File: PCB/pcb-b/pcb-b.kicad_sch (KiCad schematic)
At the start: 25 parts, among them J1 Conn_02x05_Counter_Clockwise, J2 Conn_02x05_Counter_Clockwise, K1 HK19F-DCxxV-SHC, Q13 TPCA8120,L1Q, Q3 BC817, Q9 BC817

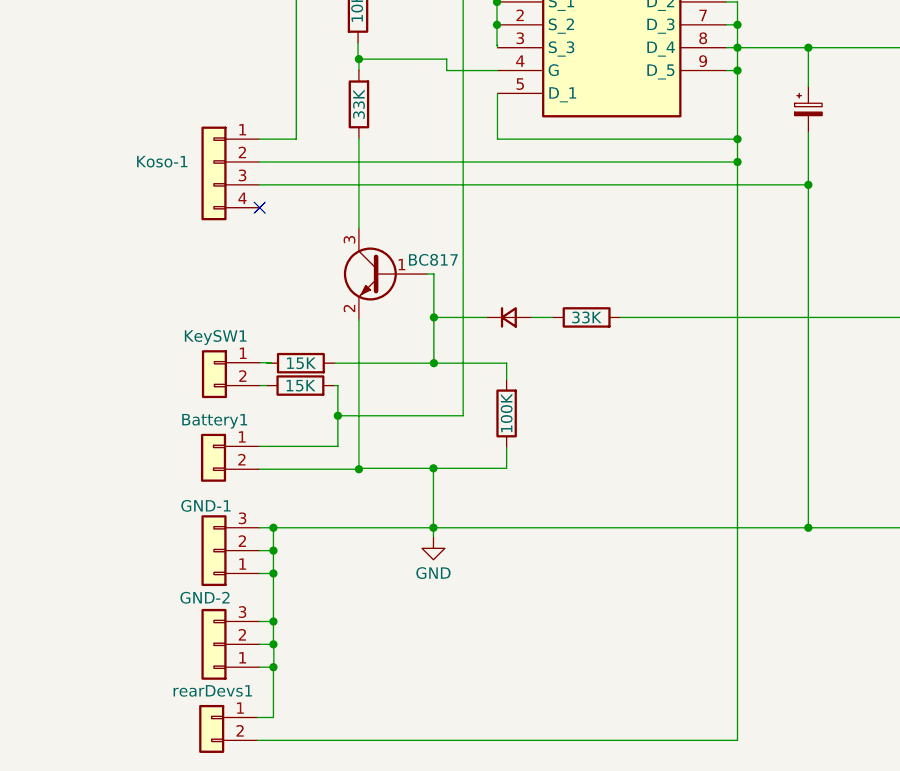
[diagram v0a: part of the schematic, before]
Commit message: Enhancements and size reduction
- Because the day-light needs just low current (<=500 mA), it no more uses the passive fuse. It has been replaced by a
  MSMF050-2 electronic fuse. Less passive fuses means less electric wires, then less chaos!
- A better components space distribution has reduced the PCB size (40.00mm x 90.11mm)
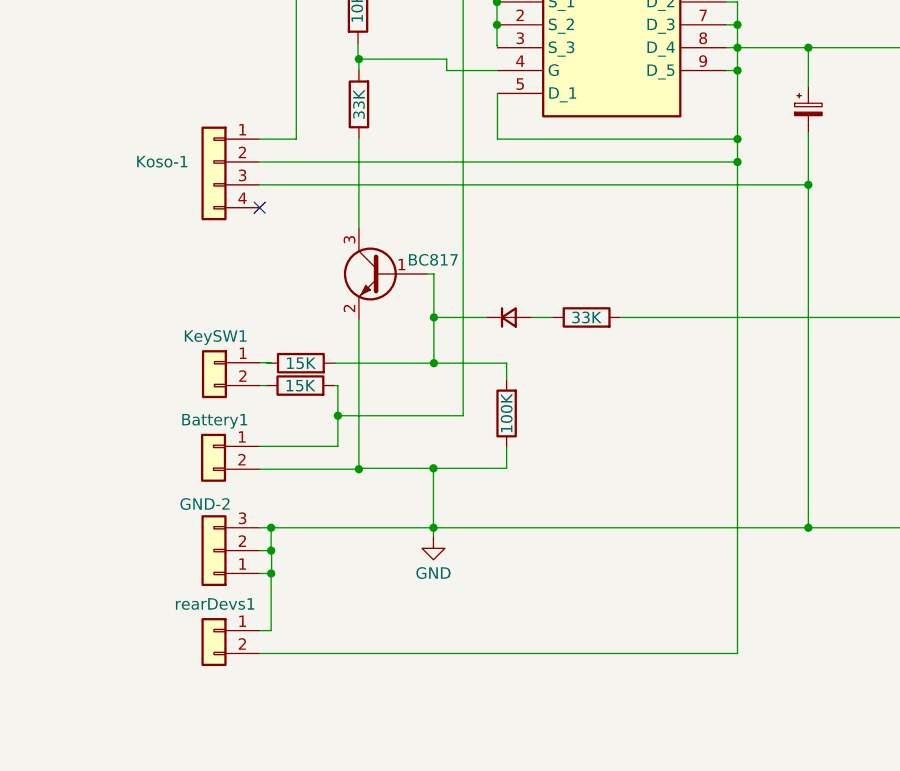
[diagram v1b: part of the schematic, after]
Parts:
- removed GND-1: ~, Connector_Wire:SolderWire-1sqmm_1x03_P5.4mm_D1.4mm_OD2.7mm, symbol Connector_Generic:Conn_01x03
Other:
- moved on the sheet: GND-2, rearDevs1
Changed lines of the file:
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@@
 	)
 	(junction
-		(at 45.72 169.164)
+		(at 45.466 158.75)
 		(diameter 0)
 		(color 0 0 0 0)
@@
 	)
 	(junction
-		(at 45.72 161.29)
-		(diameter 0)
-		(color 0 0 0 0)
-	)
-	(junction
 		(at 197.104 115.316)
 		(diameter 0)
@@
 	)
 	(junction
-		(at 45.72 158.75)
-		(diameter 0)
-		(color 0 0 0 0)
-	)
-	(junction
 		(at 70.5612 100.33)
 		(diameter 0)
@@
 	)
 	(junction
-		(at 45.72 174.244)
+		(at 45.466 163.83)
 		(diameter 0)
 		(color 0 0 0 0)
@@
 	)
 	(junction
-		(at 45.72 171.704)
+		(at 45.466 161.29)
 		(diameter 0)
 		(color 0 0 0 0)
@@
 	)
 	(junction
-		(at 45.72 163.83)
-		(diameter 0)
-		(color 0 0 0 0)
-	)
-	(junction
 		(at 149.86 135.382)
 		(diameter 0)
@@
 	(wire
 		(pts
-			(xy 45.72 161.29) (xy 45.72 163.83)
-		)
-		(stroke
-			(width 0)
-			(type default)
-		)
-	)
-	(wire
-		(pts
 			(xy 55.118 96.266) (xy 67.056 96.266)
 		)
@@
 	(wire
 		(pts
-			(xy 45.72 158.75) (xy 63.5 158.75)
-		)
-		(stroke
-			(width 0)
-			(type default)
-		)
-	)
-	(wire
-		(pts
 			(xy 107.696 77.47) (xy 107.696 77.724)
 		)
@@
 	(wire
 		(pts
-			(xy 45.72 174.244) (xy 45.7708 174.244)
+			(xy 45.466 163.83) (xy 45.5168 163.83)
 		)
 		(stroke
@@
 	(wire
 		(pts
-			(xy 116.1288 59.436) (xy 119.888 59.436)
+			(xy 45.466 158.75) (xy 63.5 158.75)
 		)
 		(stroke
@@
 	(wire
 		(pts
-			(xy 147.32 54.102) (xy 147.32 54.356)
+			(xy 116.1288 59.436) (xy 119.888 59.436)
 		)
 		(stroke
@@
 	(wire
 		(pts
-			(xy 105.156 114.808) (xy 105.156 120.65)
+			(xy 147.32 54.102) (xy 147.32 54.356)
 		)
 		(stroke
@@
 	(wire
 		(pts
-			(xy 106.934 80.01) (xy 119.888 80.01)
+			(xy 105.156 114.808) (xy 105.156 120.65)
 		)
 		(stroke
@@
 	(wire
 		(pts
-			(xy 45.72 158.75) (xy 45.72 161.29)
+			(xy 106.934 80.01) (xy 119.888 80.01)
 		)
 		(stroke
@@
 	(wire
 		(pts
-			(xy 44.196 174.244) (xy 45.72 174.244)
+			(xy 44.196 163.83) (xy 45.466 163.83)
 		)
 		(stroke
@@
 	(wire
 		(pts
-			(xy 45.72 169.164) (xy 45.72 171.704)
+			(xy 45.466 158.75) (xy 45.466 161.29)
 		)
 		(stroke
@@
 	(wire
 		(pts
-			(xy 44.196 171.704) (xy 45.72 171.704)
+			(xy 44.196 161.29) (xy 45.466 161.29)
 		)
 		(stroke
@@
 	(wire
 		(pts
-			(xy 97.282 182.372) (xy 43.942 182.372)
+			(xy 97.282 172.72) (xy 44.196 172.72)
 		)
 		(stroke
@@
 	(wire
 		(pts
-			(xy 45.72 179.832) (xy 45.72 174.244)
+			(xy 45.466 170.18) (xy 45.466 163.83)
 		)
 		(stroke
@@
 	(wire
 		(pts
-			(xy 45.7708 171.8564) (xy 45.72 171.8564)
+			(xy 45.5168 161.4424) (xy 45.466 161.4424)
 		)
 		(stroke
@@
 	(wire
 		(pts
-			(xy 44.196 161.29) (xy 45.72 161.29)
-		)
-		(stroke
-			(width 0)
-			(type default)
-		)
-	)
-	(wire
-		(pts
 			(xy 149.86 75.184) (xy 151.13 75.184)
 		)
@@
 	(wire
 		(pts
-			(xy 45.72 171.704) (xy 45.72 171.8564)
+			(xy 45.466 161.29) (xy 45.466 161.4424)
 		)
 		(stroke
@@
 	(wire
 		(pts
-			(xy 45.72 163.83) (xy 45.72 169.164)
-		)
-		(stroke
-			(width 0)
-			(type default)
-		)
-	)
-	(wire
-		(pts
 			(xy 102.616 64.262) (xy 113.538 64.262)
 		)
@@
 	(wire
 		(pts
-			(xy 44.196 169.164) (xy 45.72 169.164)
+			(xy 44.196 158.75) (xy 45.466 158.75)
 		)
 		(stroke
@@
 	(wire
 		(pts
-			(xy 43.942 179.832) (xy 45.72 179.832)
+			(xy 44.196 170.18) (xy 45.466 170.18)
 		)
 		(stroke
@@
 	(wire
 		(pts
-			(xy 97.282 118.11) (xy 97.282 182.372)
-		)
-		(stroke
-			(width 0)
-			(type default)
-		)
-	)
-	(wire
-		(pts
-			(xy 44.196 158.75) (xy 45.72 158.75)
+			(xy 97.282 118.11) (xy 97.282 172.72)
 		)
 		(stroke
@@
 	(wire
 		(pts
-			(xy 44.196 163.83) (xy 45.72 163.83)
-		)
-		(stroke
-			(width 0)
-			(type default)
-		)
-	)
-	(wire
-		(pts
-			(xy 45.7708 174.244) (xy 45.7708 171.8564)
+			(xy 45.5168 163.83) (xy 45.5168 161.4424)
 		)
 		(stroke
@@
 	)
 	(symbol
-		(lib_id "Connector_Generic:Conn_01x03")
-		(at 39.116 161.29 180)
-		(unit 1)
-		(exclude_from_sim no)
-		(in_bom yes)
-		(on_board yes)
-		(dnp no)
-		(property "Reference" "GND-1"
-			(at 38.2524 156.3624 0)
-			(effects
-				(font
-					(size 1.27 1.27)
-				)
-			)
-		)
-		(property "Value" "~"
-			(at 39.1668 156.4132 0)
-			(effects
-				(font
-					(size 1.27 1.27)
-				)
-				(hide yes)
-			)
-		)
-		(property "Footprint" "Connector_Wire:SolderWire-1sqmm_1x03_P5.4mm_D1.4mm_OD2.7mm"
-			(at 39.116 161.29 0)
-			(effects
-				(font
-					(size 1.27 1.27)
-				)
-				(hide yes)
-			)
-		)
-		(property "Datasheet" "~"
-			(at 39.116 161.29 0)
-			(effects
-				(font
-					(size 1.27 1.27)
-				)
-				(hide yes)
-			)
-		)
-		(property "Description" ""
-			(at 39.116 161.29 0)
-			(effects
-				(font
-					(size 1.27 1.27)
-				)
-				(hide yes)
-			)
-		)
-		(pin "2"
-		)
-		(pin "1"
-		)
-		(pin "3"
-		)
-		(instances
-			(project "pcb-b"
-				(path "/709d0967-afe5-49d3-92a5-d2bb94550bdb"
-					(reference "GND-1")
-					(unit 1)
-				)
-			)
-		)
-	)
-	(symbol
 		(lib_id "Device:R")
 		(at 149.86 147.574 180)
@@
 	(symbol
 		(lib_id "Connector_Generic:Conn_01x02")
-		(at 38.862 179.832 0)
+		(at 39.116 170.18 0)
 		(mirror y)
 		(unit 1)
@@
 		(dnp no)
 		(property "Reference" "rearDevs1"
-			(at 38.989 176.911 0)
+			(at 39.243 167.259 0)
 			(effects
 				(font
@@
 		)
 		(property "Value" "Conn_01x02"
-			(at 38.862 176.276 0)
+			(at 39.116 166.624 0)
 			(effects
 				(font
@@
 		)
 		(property "Footprint" "Connector_PinHeader_2.54mm:PinHeader_1x02_P2.54mm_Vertical"
-			(at 38.862 179.832 0)
+			(at 39.116 170.18 0)
 			(effects
 				(font
@@
 		)
 		(property "Datasheet" "~"
-			(at 38.862 179.832 0)
+			(at 39.116 170.18 0)
 			(effects
 				(font
@@
 		)
 		(property "Description" ""
-			(at 38.862 179.832 0)
+			(at 39.116 170.18 0)
 			(effects
 				(font
@@
 	(symbol
 		(lib_id "Connector_Generic:Conn_01x03")
-		(at 39.116 171.704 180)
+		(at 39.116 161.29 180)
 		(unit 1)
 		(exclude_from_sim no)
@@
 		(dnp no)
 		(property "Reference" "GND-2"
-			(at 38.1508 166.5732 0)
+			(at 38.1508 156.1592 0)
 			(effects
 				(font
@@
 		)
 		(property "Value" "~"
-			(at 39.1668 166.8272 0)
+			(at 39.1668 156.4132 0)
 			(effects
 				(font
@@
 		)
 		(property "Footprint" "Connector_Wire:SolderWire-0.75sqmm_1x03_P4.8mm_D1.25mm_OD2.3mm"
-			(at 39.116 171.704 0)
+			(at 39.116 161.29 0)
 			(effects
 				(font
@@
 		)
 		(property "Datasheet" "~"
-			(at 39.116 171.704 0)
+			(at 39.116 161.29 0)
 			(effects
 				(font
@@
 		)
 		(property "Description" ""
-			(at 39.116 171.704 0)
+			(at 39.116 161.29 0)
 			(effects
 				(font

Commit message: Battery connector-wire size changed
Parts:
- Battery1: footprint Connector_Wire:SolderWire-0.75sqmm_1x02_P7mm_D1.25mm_OD3.5mm -> Connector_Wire:SolderWire-1sqmm_1x02_P5.4mm_D1.4mm_OD2.7mm
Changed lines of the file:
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@@
 			)
 		)
-		(property "Footprint" "Connector_Wire:SolderWire-0.75sqmm_1x02_P7mm_D1.25mm_OD3.5mm"
+		(property "Footprint" "Connector_Wire:SolderWire-1sqmm_1x02_P5.4mm_D1.4mm_OD2.7mm"
 			(at 39.0652 149.7076 0)
 			(effects

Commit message: PCB(b) size reduction and unuseful resistors removed
Originally, I placed resistors between the MOSFET's gate and the NPN collector to reduce the possible VGS voltage difference.
But, reading the TCPA8120's datasheet I have seen it accepts VGS max -20!! But in motorbike battey I never see 20 volts. So,
I removed the resistors. Now, when the NPN is conducing then the VGS will be about -12 volts, it is also better to avoid the
MOSFETs work in linear mode.

Thank to this component removing, also the PCB size has been reduced (85.6mm x 40.0mm). But, in order to get the size reduction
the add-light connector has been splitted in two single wite connectors. It is not beautiful to see, bet the PCB size is a too
big problem, and multilayer solution is a too expensive one!
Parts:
- removed R3: 33K, Resistor_SMD:R_1206_3216Metric, symbol Device:R
- R2: value 10K -> 15K
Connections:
- net at Q13.4 (G), R2.2: now also Q9.3 (C)
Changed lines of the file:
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@@
 	)
 	(junction
+		(at 55.372 96.266)
+		(diameter 0)
+		(color 0 0 0 0)
+	)
+	(junction
 		(at 241.554 130.556)
 		(diameter 0)
@@
 	)
 	(junction
-		(at 45.466 163.83)
+		(at 55.2704 152.2476)
 		(diameter 0)
 		(color 0 0 0 0)
 	)
 	(junction
-		(at 145.288 59.69)
+		(at 45.466 163.83)
 		(diameter 0)
 		(color 0 0 0 0)
 	)
 	(junction
-		(at 45.466 161.29)
+		(at 145.288 59.69)
 		(diameter 0)
 		(color 0 0 0 0)
 	)
 	(junction
-		(at 63.5508 140.462)
+		(at 45.466 161.29)
 		(diameter 0)
 		(color 0 0 0 0)
 	)
 	(junction
-		(at 55.118 96.266)
+		(at 63.5508 140.462)
 		(diameter 0)
 		(color 0 0 0 0)
@@
 	)
 	(junction
-		(at 97.282 118.11)
+		(at 55.372 106.68)
 		(diameter 0)
 		(color 0 0 0 0)
 	)
 	(junction
-		(at 55.2196 106.68)
+		(at 97.282 118.11)
 		(diameter 0)
 		(color 0 0 0 0)
@@
 	)
 	(junction
-		(at 55.2196 152.2476)
-		(diameter 0)
-		(color 0 0 0 0)
-	)
-	(junction
 		(at 97.282 115.57)
 		(diameter 0)
@@
 	(wire
 		(pts
-			(xy 55.2704 152.2476) (xy 55.2196 152.2476)
-		)
-		(stroke
-			(width 0)
-			(type default)
-		)
-	)
-	(wire
-		(pts
 			(xy 138.684 77.978) (xy 138.684 77.47)
 		)
@@
 	(wire
 		(pts
-			(xy 55.118 96.266) (xy 67.056 96.266)
-		)
-		(stroke
-			(width 0)
-			(type default)
-		)
-	)
-	(wire
-		(pts
 			(xy 147.828 74.93) (xy 132.588 74.93)
 		)
@@
 	(wire
 		(pts
-			(xy 55.2196 106.68) (xy 55.2196 107.8992)
-		)
-		(stroke
-			(width 0)
-			(type default)
-		)
-	)
-	(wire
-		(pts
 			(xy 254.508 98.298) (xy 218.694 98.298)
 		)
@@
 	(wire
 		(pts
-			(xy 55.118 104.902) (xy 55.118 106.68)
+			(xy 55.372 105.156) (xy 55.372 106.68)
 		)
 		(stroke
@@
 	(wire
 		(pts
-			(xy 55.118 94.996) (xy 55.118 96.266)
+			(xy 55.372 96.266) (xy 67.056 96.266)
+		)
+		(stroke
+			(width 0)
+			(type default)
+		)
+	)
+	(wire
+		(pts
+			(xy 55.372 94.996) (xy 55.372 96.266)
 		)
 		(stroke
@@
 	(wire
 		(pts
-			(xy 44.1452 152.2476) (xy 55.2196 152.2476)
+			(xy 44.1452 152.2476) (xy 55.2704 152.2476)
 		)
 		(stroke
@@
 	(wire
 		(pts
-			(xy 64.9732 106.68) (xy 55.2196 106.68)
+			(xy 64.9732 106.68) (xy 55.372 106.68)
 		)
 		(stroke
@@
 	(wire
 		(pts
-			(xy 55.118 106.68) (xy 55.2196 106.68)
-		)
-		(stroke
-			(width 0)
-			(type default)
-		)
-	)
-	(wire
-		(pts
-			(xy 55.2196 115.5192) (xy 55.2196 125.476)
-		)
-		(stroke
-			(width 0)
-			(type default)
-		)
-	)
-	(wire
-		(pts
 			(xy 145.288 59.69) (xy 151.13 59.69)
 		)
@@
 	(wire
 		(pts
-			(xy 63.5508 130.556) (xy 63.5508 135.382)
+			(xy 63.5508 130.302) (xy 63.5508 135.382)
 		)
 		(stroke
@@
 	(wire
 		(pts
-			(xy 55.2196 135.636) (xy 55.2196 152.2476)
+			(xy 55.372 135.382) (xy 55.372 152.2476)
 		)
 		(stroke
@@
 	(wire
 		(pts
-			(xy 55.118 96.266) (xy 55.118 97.282)
+			(xy 55.372 96.266) (xy 55.372 97.536)
 		)
 		(stroke
@@
 	(wire
 		(pts
-			(xy 48.26 96.266) (xy 55.118 96.266)
+			(xy 48.26 96.266) (xy 55.372 96.266)
 		)
 		(stroke
@@
 	(wire
 		(pts
-			(xy 63.5508 130.556) (xy 62.8396 130.556)
+			(xy 63.5508 130.302) (xy 62.992 130.302)
 		)
 		(stroke
@@
 	(wire
 		(pts
+			(xy 55.372 152.2476) (xy 55.2704 152.2476)
+		)
+		(stroke
+			(width 0)
+			(type default)
+		)
+	)
+	(wire
+		(pts
 			(xy 44.196 158.75) (xy 45.466 158.75)
 		)
@@
 	(wire
 		(pts
+			(xy 55.372 106.68) (xy 55.372 125.222)
+		)
+		(stroke
+			(width 0)
+			(type default)
+		)
+	)
+	(wire
+		(pts
 			(xy 52.578 140.462) (xy 63.5508 140.462)
 		)
@@
 	(symbol
 		(lib_id "power:+12V")
-		(at 55.118 94.996 0)
+		(at 55.372 94.996 0)
 		(unit 1)
 		(exclude_from_sim no)
@@
 		(dnp no)
 		(property "Reference" "#PWR0101"
-			(at 55.118 98.806 0)
+			(at 55.372 98.806 0)
 			(effects
 				(font
@@
 		)
 		(property "Value" "+12V"
-			(at 55.118 90.805 0)
+			(at 55.372 90.805 0)
 			(effects
 				(font
@@
 		)
 		(property "Footprint" ""
-			(at 55.118 94.996 0)
+			(at 55.372 94.996 0)
 			(effects
 				(font
@@
 		)
 		(property "Datasheet" ""
-			(at 55.118 94.996 0)
+			(at 55.372 94.996 0)
 			(effects
 				(font
@@
 		)
 		(property "Description" ""
-			(at 55.118 94.996 0)
+			(at 55.372 94.996 0)
 			(effects
 				(font
@@
 	(symbol
 		(lib_id "Transistor_BJT:BC817")
-		(at 57.7596 130.556 0)
+		(at 57.912 130.302 0)
 		(mirror y)
 		(unit 1)
@@
 		(dnp no)
 		(property "Reference" "Q9"
-			(at 51.816 129.286 0)
+			(at 51.9684 129.032 0)
 			(effects
 				(font
@@
 		)
 		(property "Value" "BC817"
-			(at 66.3448 129.032 0)
+			(at 66.4972 128.778 0)
 			(effects
 				(font
@@
 		)
 		(property "Footprint" "Package_TO_SOT_SMD:SOT-23"
-			(at 52.6796 132.461 0)
+			(at 52.832 132.207 0)
 			(effects
 				(font
@@
 		)
 		(property "Datasheet" "https://www.onsemi.com/pub/Collateral/BC818-D.pdf"
-			(at 57.7596 130.556 0)
+			(at 57.912 130.302 0)
 			(effects
 				(font
@@
 		)
 		(property "Description" ""
-			(at 57.7596 130.556 0)
+			(at 57.912 130.302 0)
 			(effects
 				(font
@@
 	(symbol
 		(lib_id "Device:R")
-		(at 55.2196 111.7092 180)
-		(unit 1)
-		(exclude_from_sim no)
-		(in_bom yes)
-		(on_board yes)
-		(dnp no)
-		(property "Reference" "R3"
-			(at 48.9204 111.7092 90)
-			(effects
-				(font
-					(size 1.27 1.27)
-				)
-				(hide yes)
-			)
-		)
-		(property "Value" "33K"
-			(at 55.2704 111.76 90)
-			(effects
-				(font
-					(size 1.27 1.27)
-				)
-			)
-		)
-		(property "Footprint" "Resistor_SMD:R_1206_3216Metric"
-			(at 56.9976 111.7092 90)
-			(effects
-				(font
-					(size 1.27 1.27)
-				)
-				(hide yes)
-			)
-		)
-		(property "Datasheet" "~"
-			(at 55.2196 111.7092 0)
-			(effects
-				(font
-					(size 1.27 1.27)
-				)
-				(hide yes)
-			)
-		)
-		(property "Description" ""
-			(at 55.2196 111.7092 0)
-			(effects
-				(font
-					(size 1.27 1.27)
-				)
-				(hide yes)
-			)
-		)
-		(pin "1"
-		)
-		(pin "2"
-		)
-		(instances
-			(project "pcb-b"
-				(path "/709d0967-afe5-49d3-92a5-d2bb94550bdb"
-					(reference "R3")
-					(unit 1)
-				)
-			)
-		)
-	)
-	(symbol
-		(lib_id "Device:R")
 		(at 48.768 140.462 90)
 		(unit 1)
@@
 	(symbol
 		(lib_id "Device:R")
-		(at 55.118 101.092 0)
+		(at 55.372 101.346 0)
 		(unit 1)
 		(exclude_from_sim no)
@@
 		(dnp no)
 		(property "Reference" "R2"
-			(at 61.4172 101.092 90)
+			(at 61.6712 101.346 90)
 			(effects
 				(font
@@
 			)
 		)
-		(property "Value" "10K"
-			(at 55.0672 101.0412 90)
+		(property "Value" "15K"
+			(at 55.3212 101.2952 90)
 			(effects
 				(font
@@
 		)
 		(property "Footprint" "Resistor_SMD:R_1206_3216Metric"
-			(at 53.34 101.092 90)
+			(at 53.594 101.346 90)
 			(effects
 				(font
@@
 		)
 		(property "Datasheet" "~"
-			(at 55.118 101.092 0)
+			(at 55.372 101.346 0)
 			(effects
 				(font
@@
 		)
 		(property "Description" ""
-			(at 55.118 101.092 0)
+			(at 55.372 101.346 0)
 			(effects
 				(font

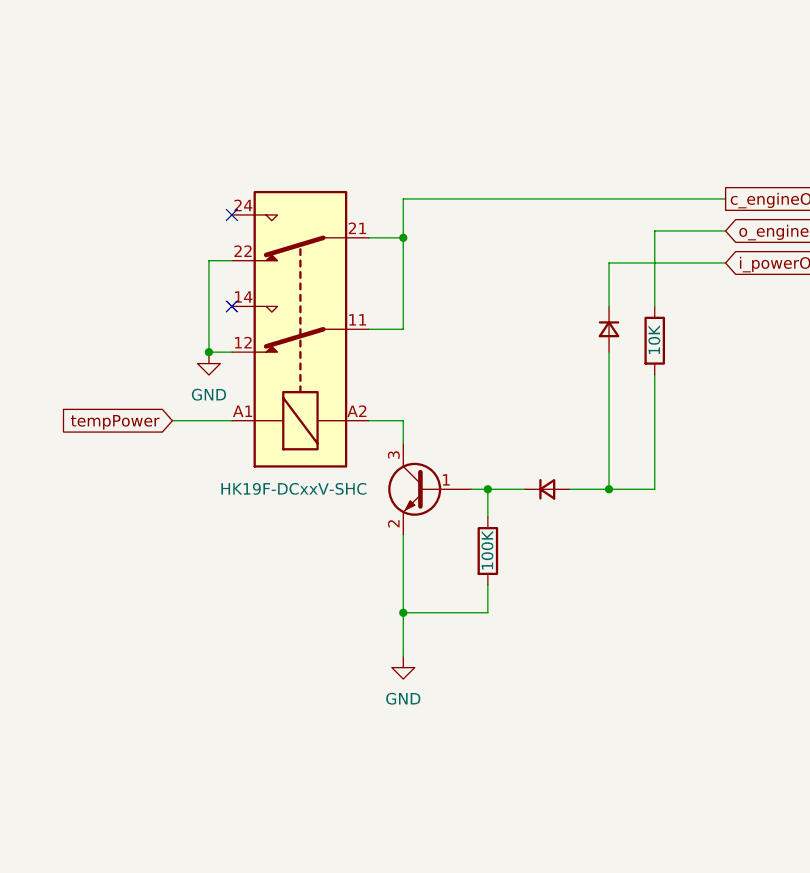
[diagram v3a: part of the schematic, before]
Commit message: Flyback diode added
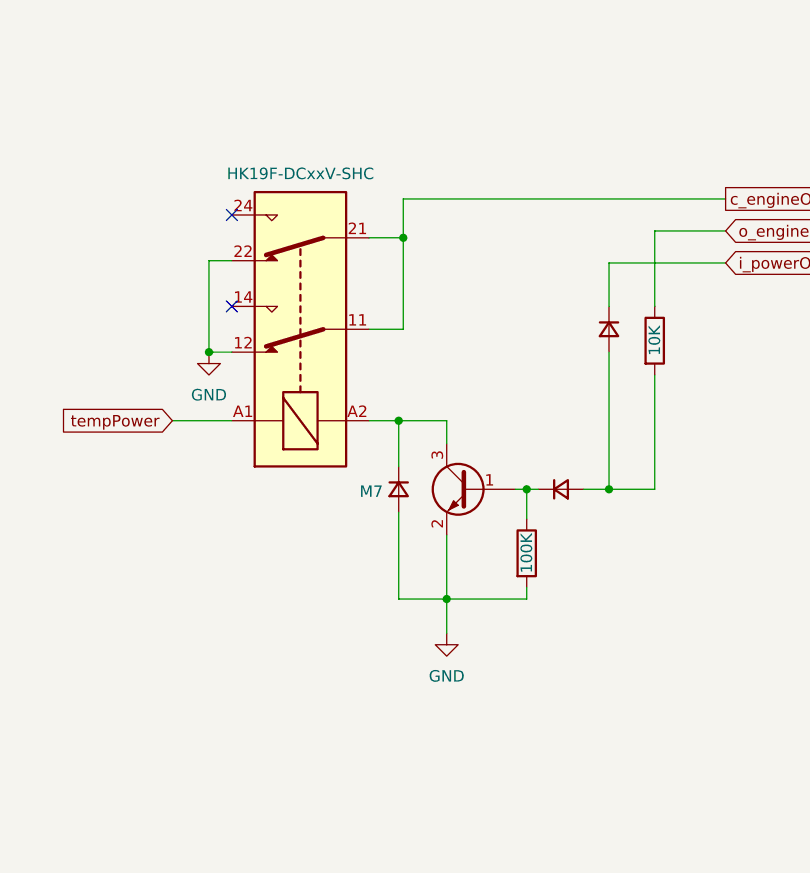
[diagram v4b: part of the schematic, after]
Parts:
- added flyback-1: M7, Diode_SMD:D_2114_3652Metric_Pad1.85x3.75mm_HandSolder, symbol Device:D_Small
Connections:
- net GND: now also flyback-1.2 (A)
- net at K1.A2, Q3.3 (C): now also flyback-1.1 (K)
